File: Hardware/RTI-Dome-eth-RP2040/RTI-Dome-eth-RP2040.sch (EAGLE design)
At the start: 112 parts, among them IC1 RP2040, IC2 24LC128T-I_SN, IC3 FT232RL, IC5 74LVC245, IC6 74ABT245, IC7 W25Q128JVSIM_TR, IC8 REG1117-3.3V, IC9 REG1117-5V, J1 47642-1001, J2 XT60PW-M, U1 W5500, X13 PN61729-S, X9 J1011F21PNL

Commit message: Fix packages for ABT abd LVC buffers
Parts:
- IC5: MPN 74LVC245APW,112 -> (none)
- IC6: MPN 74ABT245PW,112 -> (none)
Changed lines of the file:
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@@
 </part>
 <part name="FRAME1" library="frames" library_urn="urn:adsk.eagle:library:229" deviceset="DINA3_L" device=""/>
-<part name="IC5" library="rti" library_urn="urn:adsk.eagle:library:37256580" deviceset="74*245" device="" package3d_urn="urn:adsk.eagle:package:37318379/2" technology="LVC">
-<attribute name="MPN" value="74LVC245APW,112"/>
-</part>
-<part name="IC6" library="rti" library_urn="urn:adsk.eagle:library:37256580" deviceset="74*245" device="" package3d_urn="urn:adsk.eagle:package:37318379/2" technology="ABT" value="74ABT245">
-<attribute name="MPN" value="74ABT245PW,112"/>
-</part>
+<part name="IC5" library="rti" library_urn="urn:adsk.eagle:library:37256580" deviceset="74*245" device="" package3d_urn="urn:adsk.eagle:package:37318379/2" technology="LVC"/>
+<part name="IC6" library="rti" library_urn="urn:adsk.eagle:library:37256580" deviceset="74*245" device="" package3d_urn="urn:adsk.eagle:package:37318379/2" technology="ABT" value="74ABT245"/>
 <part name="GND7" library="supply1" library_urn="urn:adsk.eagle:library:371" deviceset="GND" device=""/>
 <part name="U1" library="W5500" library_urn="urn:adsk.eagle:library:37501005" deviceset="W5500" device="" package3d_urn="urn:adsk.eagle:package:37501008/2" value="W5500">

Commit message: Some addition small fixes to Firmware on RP2040. Tested and working.
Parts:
- added C40, C41, C42, C43, C44, C45, C46: 10uF, rcl:C-EUC0805
- added R44, R45, R46, R47, R48, R49, R50: 100, rcl:R-EU_R0805
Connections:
- removed net AT_PARK_PIN_EXT: IC5G$1.A7, R20.1, X7-2.KL
- removed net BUTTON_WEST_CLOSE_5V: IC5G$1.A2, R15.2, X4-3.KL
- removed net HOME_SHUTTER_CLOSED_5V: IC5G$1.A1, R18.2, X1-2.KL
- removed net SHUTTER_OPENED_5V: IC5G$1.A6, R17.2, X3-2.KL
- removed net SPARE1_EXT: IC5G$1.A0, R21.2, X8-1.KL
- removed net SPARE2_EXT: IC5G$1.A4, R9.2, X8-2.KL
- new net AT_PARK_PIN-IN_EXT: R46.2, X7-2.KL
- new net AT_PARK_PIN_IN_5V: C42.1, IC5G$1.A7, R20.1, R46.1
- new net BUTTON_EAST_OPEN-IN_EXT: R44.2, X4-2.KL
- new net BUTTON_WEST_CLOSE-IN_EXT: R47.2, X4-3.KL
- new net BUTTON_WEST_CLOSE_IN_5V: C43.1, IC5G$1.A2, R15.2, R47.1
- new net HOME_SHUTTER_CLOSED-IN_EXT: R50.2, X1-2.KL
- new net HOME_SHUTTER_CLOSED_IN_5V: C46.1, IC5G$1.A1, R18.2, R50.1
- new net SHUTTER_OPENED-IN_EXT: R48.2, X3-2.KL
- new net SHUTTER_OPENED_IN_5V: C44.1, IC5G$1.A6, R17.2, R48.1
- new net SPARE1-IN_EXT: R45.2, X8-1.KL
- new net SPARE1_IN_5V: C41.1, IC5G$1.A0, R21.2, R45.1
- new net SPARE2-IN_EXT: R49.2, X8-2.KL
- new net SPARE2_IN_5V: C45.1, IC5G$1.A4, R49.1, R9.2
- net BUTTON_EAST_OPEN_5V: now also C40.1, R44.1; no longer X4-2.KL
- net GND: now also C40.2, C41.2, C42.2, C43.2, C44.2, C45.2, C46.2
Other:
- moved on the sheet: C1, R4, R5, X10-1, X10-2, X10-3, X2-1, X2-2, X2-3, X7-1, X7-2, X7-3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

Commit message: Set the shuuter response to open when there is no shutter controler
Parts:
- removed 12MHZ: CB3LV-OSCILATOR, rti:CB3LV-OSCILATOR
- removed BOOT_SEL: (no value), switch-omron:10-XX
- removed C25, C26, C29, C30, C31, C32, C33, C34, C35, C37, C38: 100nF, rcl:C-EUC0805
- removed C36, C39: 2.2uF, rcl:C-EUC0805
- removed IC1: RP2040, samacsys:RP2040
- removed IC7: W25Q128JVSIM_TR, samacsys:W25Q128JVSIM_TR
- removed J1: 47642-1001, samacsys:47642-1001
- removed R22, R41: 27.4, rcl:R-EU_R0805
- removed R42: 10K, rcl:R-EU_R0805
- removed R43: 1k, rcl:R-EU_R0805
- added IC4: RASPBERRY_PI_PICO, samacsys:RASPBERRY_PI_PICO
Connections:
- net USBDM renamed USBD_N
- net USBDP renamed USBD_P
- removed net $N38: IC1.GPIO23
- removed net 1.1V: C37.1, C38.1, C39.1, IC1.DVDD_1, IC1.DVDD_2, IC1.VREG_VOUT
- removed net CLOCK_IN: 12MHZ.FO, IC1.XIN
- removed net N$1: IC1.GPIO24
- removed net N$14: J1.3, R22.2
- removed net N$16: BOOT_SEL.S, BOOT_SEL.S1, R43.1
- removed net N$39: IC1.GPIO25
- removed net N$4: J1.2, R41.2
- removed net N$40: IC1.GPIO27/ADC1
- removed net N$42: IC1.GPIO29/ADC3
- removed net QSPI_CS: IC1.QSPI_SS_N, IC7./CS, R42.2, R43.2
- removed net QSPI_SCLK: IC1.QSPI_SCLK, IC7.CLK
- removed net QSPI_SD0: IC1.QSPI_SD0, IC7.DI_(IO0)
- removed net QSPI_SD1: IC1.QSPI_SD1, IC7.DO_(IO1)
- removed net QSPI_SD2: IC1.QSPI_SD2, IC7./WP_(IO2)
- removed net QSPI_SD3: IC1.QSPI_SD3, IC7./HOLD_OR_/RESET_(IO3)
- removed net USB_DM: IC1.USB_DM, R41.1
- removed net USB_DP: IC1.USB_DP, R22.1
- new net N$56: IC4.I2C1_SCL_/ADC1/GP_27
- new net N$59: IC4.ADC_VREF
- new net N$60: IC4.3V3(OUT)
- new net N$61: IC4.3V3_EN
- new net N$64: IC4.VBUS
- net 3.3V: no longer 12MHZ.OE, 12MHZ.VDD, C25.1, C26.1, C29.1, C30.1, C31.1, C32.1, C33.1, C34.1, C35.1, C36.1, IC1.ADC_AVDD, IC1.IOVDD_1, IC1.IOVDD_2, IC1.IOVDD_3, IC1.IOVDD_4, IC1.IOVDD_5, IC1.IOVDD_6, IC1.USB_VDD, IC1.VREG_VIN, IC7.VCC, R42.1
- net AT_PARK_PIN: now also IC4.I2C1_SCL/SPI1_TX/GP15; no longer IC1.GPIO15
- net BUTTON_EAST_OPEN: now also IC4.I2C1_SCL_/SPI1__TX/GP11; no longer IC1.GPIO11
- net BUTTON_WEST_CLOSE: now also IC4.I2C1_SDA_/SPI1__SCK/GP10; no longer IC1.GPIO10
- net ETH_CS: now also IC4.UART0_RX/I2C0_SCL/SPIO_CSN/GP17; no longer IC1.GPIO17
- net ETH_RESET: now also IC4.I2C0_SDA/GP20; no longer IC1.GPIO20
- net FTDI_RESET: now also IC4.GP28/ADC2; no longer IC1.GPIO28/ADC2
- net GND: now also IC4.GND/AGND, IC4.GND_1, IC4.GND_2, IC4.GND_3, IC4.GND_4, IC4.GND_5, IC4.GND_6, IC4.GND_7; no longer 12MHZ.GND, BOOT_SEL.P, BOOT_SEL.P1, C25.2, C26.2, C29.2, C30.2, C31.2, C32.2, C33.2, C34.2, C35.2, C36.2, C37.2, C38.2, C39.2, IC1.GND, IC7.GND, J1.5, J1.MH1, J1.MH2, J1.MH3, J1.MH4
- net HOME_SHUTTER_CLOSED: now also IC4.I2C1_SCL_/SPI0_TX/GP7; no longer IC1.GPIO7
- net M_DIR: now also IC4.I2C0_SCL_/SPI0_TX/GP3; no longer IC1.GPIO3
- net M_EN: now also IC4.I2C1_SDA_/SPI0_SCK/GP2; no longer IC1.GPIO2
- net M_STEP: now also IC4.I2C0_SCL/GP21; no longer IC1.GPIO21
- net RESET: now also IC4.RUN; no longer IC1.RUN
- net RG-11: now also IC4.UART0_RX/I2C0_SCL_/SPI1_CSN/GP13; no longer IC1.GPIO13
- net RX2: now also IC4.UART1_RX/I2C0_SCL_/SPI1_CSN/GP9; no longer IC1.GPIO9
- net SCL: now also IC4.UART1_RX/I2C0_SCL_/SPI0_CSN/GP5; no longer IC1.GPIO5
- net SCLK: now also IC4.I2C1_SDA/_SPI0_SCK/GP18; no longer IC1.GPIO18
- net SDA: now also IC4.UART1_TX/I2C0_SDA_/SPI0_RX/GP4; no longer IC1.GPIO4
- net SDI: now also IC4.UART0_TX/I2C0_SDA_/SPI0_RX_/GP16; no longer IC1.GPIO16
- net SDO: now also IC4.I2C1_SCL/_SPI0_TX/GP19; no longer IC1.GPIO19
- net SHUTTER_OPENED: now also IC4.I2C1_SDA/SPI1_SCK/GP14; no longer IC1.GPIO14
- net SPARE1: now also IC4.I2C1_SDA_/SPI0_SCK/GP6; no longer IC1.GPIO6
- net SPARE2: now also IC4.UART0_TX/I2C0_SDA_/SPI1_RX_/GP12; no longer IC1.GPIO12
- net TX2: now also IC4.UART1_TX/I2C0_SDA_/SPI1_RX/GP8; no longer IC1.GPIO8
- net VCC: now also IC4.VSYS
- net VPIN: now also IC4.I2C1_SDA/ADC0/GP26; no longer IC1.GPIO26/ADC0
- net XBEE_DIN: now also IC4.UART0_TX/I2C0_SDA_/SPI0_RX/GP0; no longer IC1.GPIO0
- net XBEE_DOUT: now also IC4.UART0_RX/I2C0_SCL_/SPI0_CSN/GP1; no longer IC1.GPIO1
- net XBEE_RESET: now also IC4.GP22; no longer IC1.GPIO22
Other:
- note removed: "Fix ADC_AVDD"
- moved on the sheet: X13

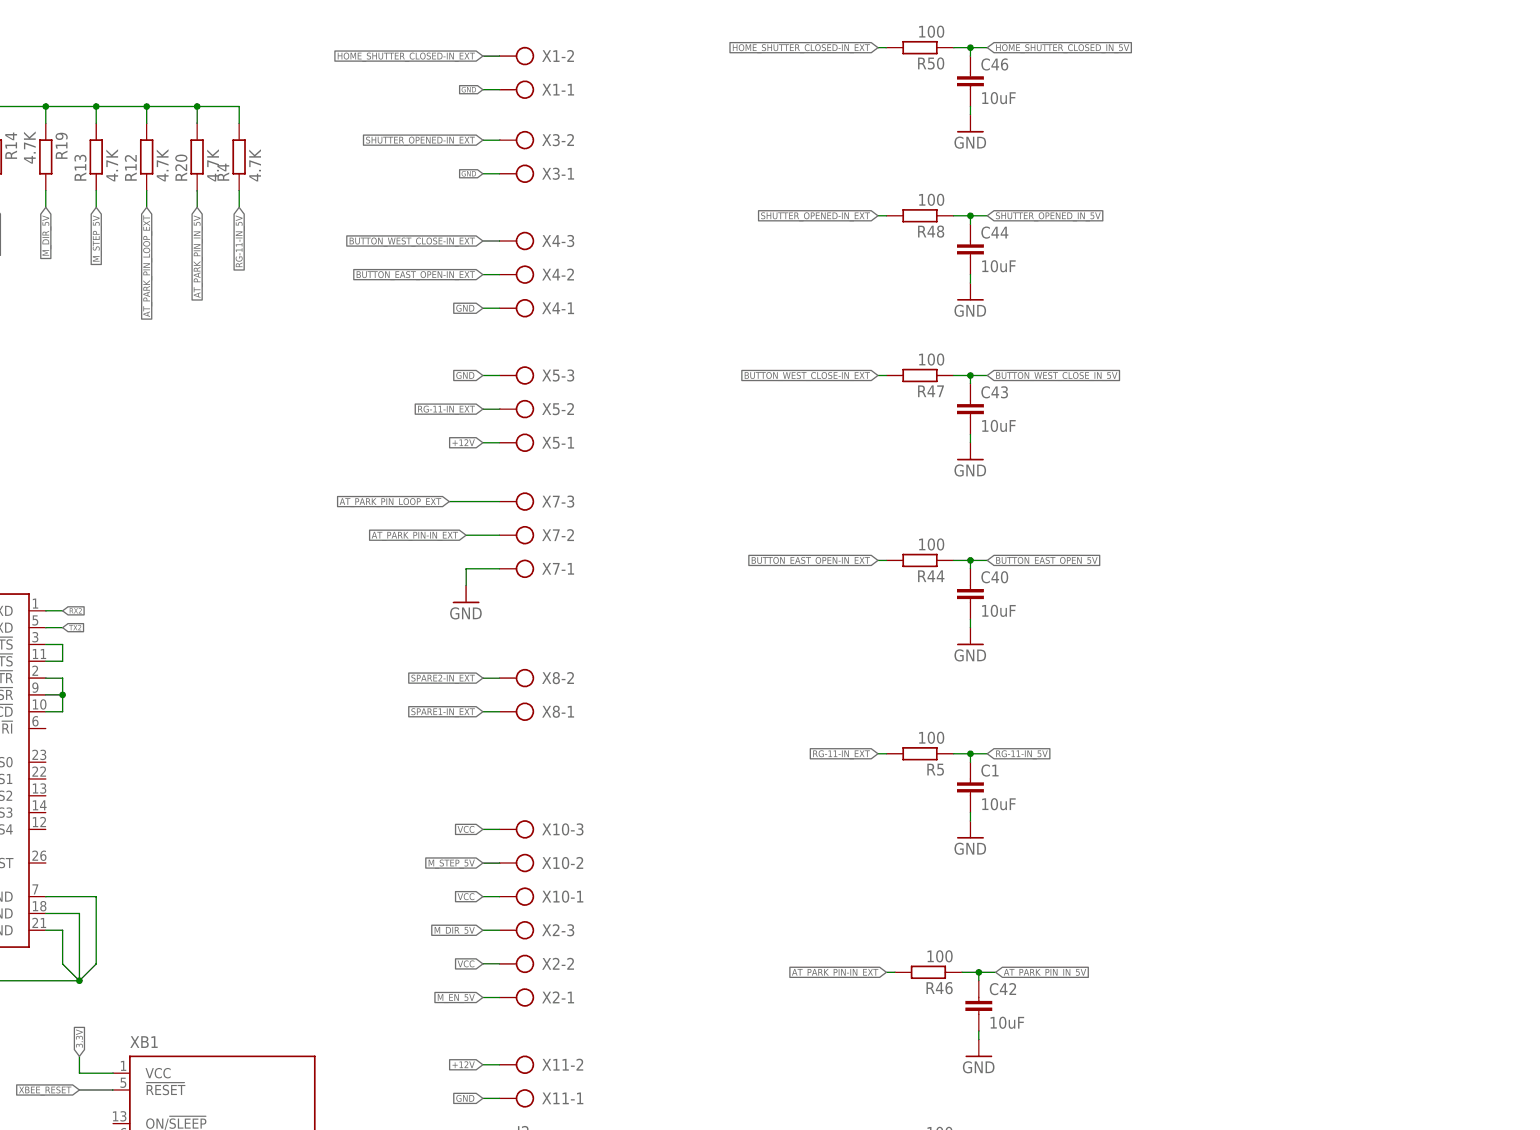
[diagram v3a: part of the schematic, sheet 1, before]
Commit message: Finished routing on RP2040 board
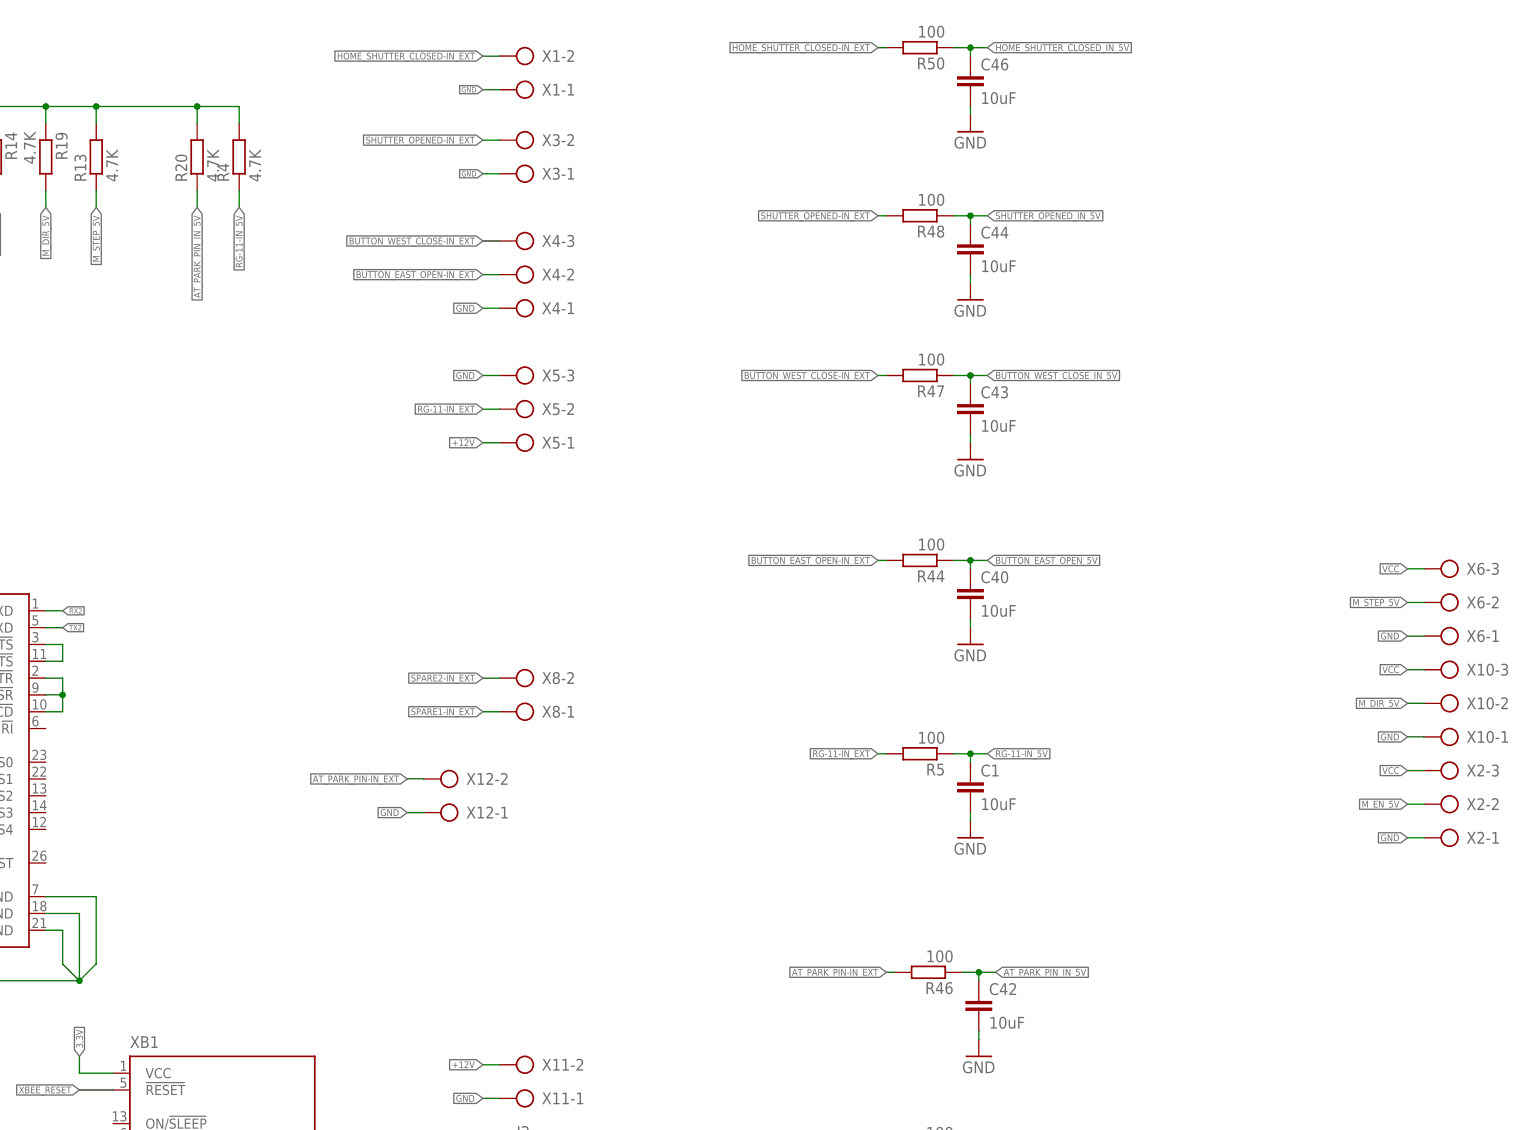
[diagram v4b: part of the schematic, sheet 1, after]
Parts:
- removed R12: 4.7K, rcl:R-EU_R0805
- removed X7: (no value), rti:AK500/3
- added X12: (no value), rti:AK500/2
- added X6: (no value), rti:AK500/3
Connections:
- net AT_PARK_PIN-IN_EXT: now also X12-2.KL; no longer X7-2.KL
- net AT_PARK_PIN_LOOP_EXT: no longer R12.1, X7-3.KL
- net GND: now also X10-1.KL, X12-1.KL, X2-1.KL, X6-1.KL; no longer X7-1.KL
- net M_DIR_5V: now also X10-2.KL; no longer X2-3.KL
- net M_EN_5V: now also X2-2.KL; no longer X2-1.KL
- net M_STEP_5V: now also X6-2.KL; no longer X10-2.KL
- net VCC: now also X2-3.KL, X6-3.KL; no longer R12.2, X10-1.KL, X2-2.KL
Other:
- moved on the sheet: X10-1, X10-2, X10-3, X2-1, X2-2, X2-3

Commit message: moved some component to avoid colisions (3D rendring helps ! )
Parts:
- removed RESET: (no value), switch-omron:10-XX
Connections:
- net GND: no longer RESET.S, RESET.S1
- net RESET: no longer RESET.P, RESET.P1
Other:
- moved on the sheet: IC4
